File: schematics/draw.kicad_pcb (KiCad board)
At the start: 2 copper layers, 50 x 40 mm, 38 parts, among them P1 I2C Conn, P2 UART Conn, P3 Debug Conn, P4 USB_OTG, P5 Power_IN, P6 Power_OUT, SW1 SW_Push, U1 EFM32HG309, U2 TPD4E002, U3 INA260

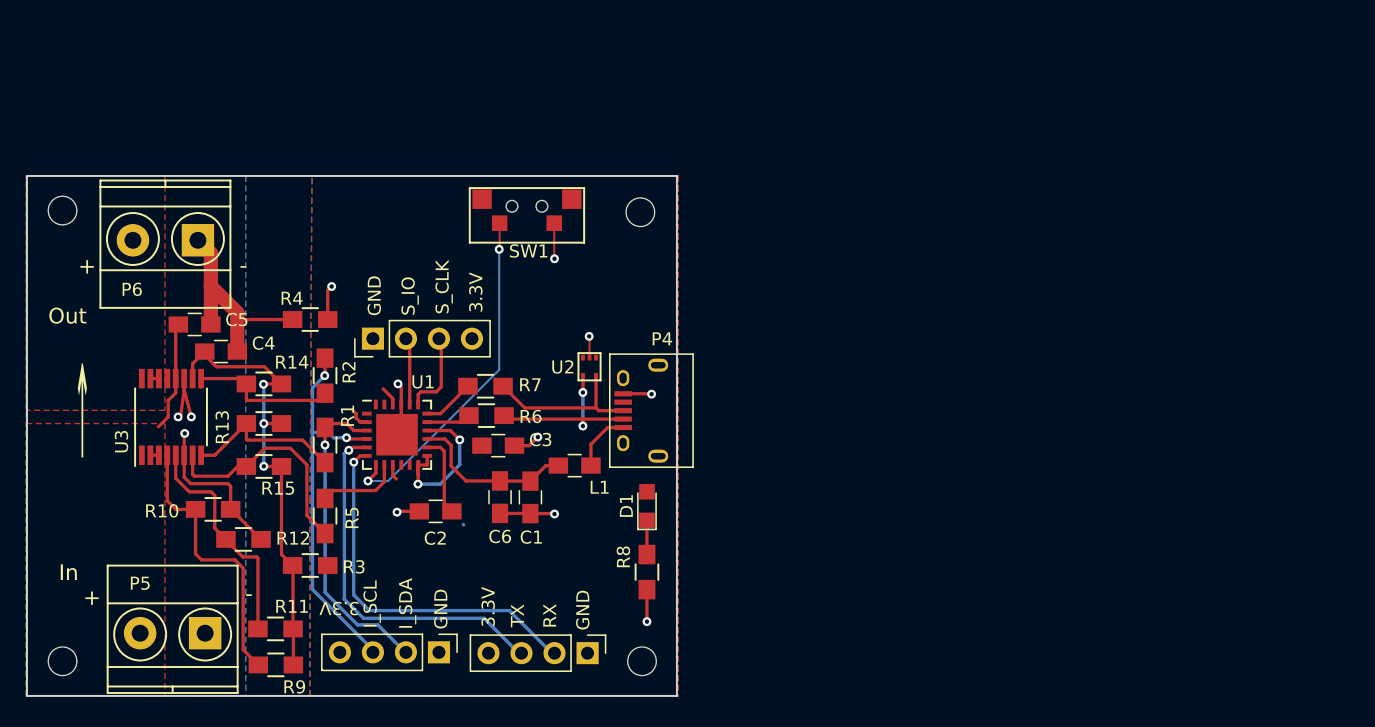
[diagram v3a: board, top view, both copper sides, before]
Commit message: updating footprint assignment
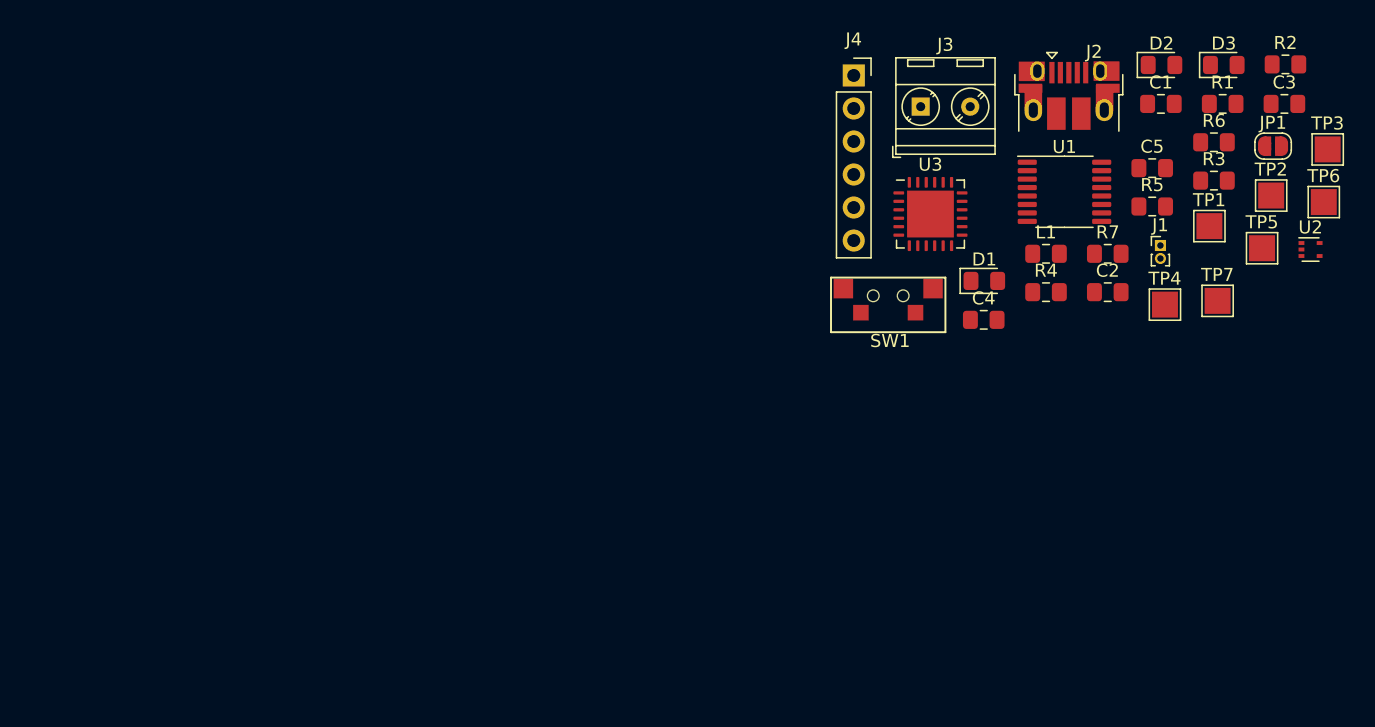
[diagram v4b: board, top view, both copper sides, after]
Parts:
- removed C6: 1nF, Capacitors_SMD:C_0805_HandSoldering
- removed P1: I2C Conn, Pin_Headers:Pin_Header_Straight_1x04_Pitch2.54mm
- removed P2: UART Conn, Pin_Headers:Pin_Header_Straight_1x04_Pitch2.54mm
- removed P3: Debug Conn, Pin_Headers:Pin_Header_Straight_1x04_Pitch2.54mm
- removed P4: USB_OTG, Connect:USB_Micro-B
- removed P5: Power_IN, Terminal_Blocks:TerminalBlock_Pheonix_MKDS1.5-2pol
- removed P6: Power_OUT, Terminal_Blocks:TerminalBlock_Pheonix_MKDS1.5-2pol
- removed R10, R12: 0R, Resistors_SMD:R_0805_HandSoldering
- removed R11, R9: 0R_NP, Resistors_SMD:R_0805_HandSoldering
- removed R13, R14, R15: 1K, Resistors_SMD:R_0805_HandSoldering
- removed R8: 100R, Resistors_SMD:R_0805_HandSoldering
- removed REF** (x4): MountingHole_2.2mm_M2, Mounting_Holes:MountingHole_2.2mm_M2
- removed REF***: OSHW-Logo_5.7x6mm_SilkScreen, Symbols:OSHW-Logo_5.7x6mm_SilkScreen
- added D2: Diode, Diode_SMD:D_0805_2012Metric_Pad1.15x1.40mm_HandSolder, F.Cu at (147.3, 86.5)
- added D3: LED, LED_SMD:LED_0805_2012Metric_Pad1.15x1.40mm_HandSolder, F.Cu at (152.1, 86.5)
- added J1: Conn_01x02_Female, Connector_PinHeader_1.00mm:PinHeader_1x02_P1.00mm_Vertical, F.Cu at (147.2, 100.3)
- added J2: USB_B_Micro, Connector_USB:USB_Micro-B_Amphenol_10103594-0001LF_Horizontal, F.Cu at (140.2, 88.8)
- added J3: Screw_Terminal_01x02, TerminalBlock_MetzConnect:TerminalBlock_MetzConnect_Type086_RT03402HBLC_1x02_P3.81mm_Horizontal, F.Cu at (128.8, 89.7)
- added J4: Debug Header, Connector_PinSocket_2.54mm:PinSocket_1x06_P2.54mm_Vertical, F.Cu at (123.6, 87.3)
- added JP1: Jumper, Jumper:SolderJumper-2_P1.3mm_Open_RoundedPad1.0x1.5mm, F.Cu at (155.9, 92.7)
- added TP1: TestPoint, TestPoint:TestPoint_Pad_2.0x2.0mm, F.Cu at (151.0, 98.9)
- added TP2: TestPoint, TestPoint:TestPoint_Pad_2.0x2.0mm, F.Cu at (155.7, 96.5)
- added TP3: TestPoint, TestPoint:TestPoint_Pad_2.0x2.0mm, F.Cu at (160.1, 93.0)
- added TP4: TestPoint, TestPoint:TestPoint_Pad_2.0x2.0mm, F.Cu at (147.5, 104.9)
- added TP5: TestPoint, TestPoint:TestPoint_Pad_2.0x2.0mm, F.Cu at (155.0, 100.6)
- added TP6: TestPoint, TestPoint:TestPoint_Pad_2.0x2.0mm, F.Cu at (159.8, 97.0)
- added TP7: TestPoint, TestPoint:TestPoint_Pad_2.0x2.0mm, F.Cu at (151.6, 104.6)
- C1: value 4.7uF -> 0.1uF; footprint Capacitors_SMD:C_0805_HandSoldering -> Capacitor_SMD:C_0805_2012Metric_Pad1.15x1.40mm_HandSolder
- C2: value 1uF -> 1nF; footprint Capacitors_SMD:C_0805_HandSoldering -> Capacitor_SMD:C_0805_2012Metric_Pad1.15x1.40mm_HandSolder
- C3: value 1uF -> 4.7uF; footprint Capacitors_SMD:C_0805_HandSoldering -> Capacitor_SMD:C_0805_2012Metric_Pad1.15x1.40mm_HandSolder
- C4: value 0.1uF -> 1uF; footprint Capacitors_SMD:C_0805_HandSoldering -> Capacitor_SMD:C_0805_2012Metric_Pad1.15x1.40mm_HandSolder
- C5: footprint Capacitors_SMD:C_0805_HandSoldering -> Capacitor_SMD:C_0805_2012Metric_Pad1.15x1.40mm_HandSolder
- D1: footprint LEDs:LED_0805 -> LED_SMD:LED_0805_2012Metric_Pad1.15x1.40mm_HandSolder
- L1: footprint Capacitors_SMD:C_0805_HandSoldering -> Inductor_SMD:L_0805_2012Metric_Pad1.15x1.40mm_HandSolder
- R1, R2: value 0R -> 15R; footprint Resistors_SMD:R_0805_HandSoldering -> Resistor_SMD:R_0805_2012Metric_Pad1.15x1.40mm_HandSolder
- R3, R4, R5: value 0R -> 4K7; footprint Resistors_SMD:R_0805_HandSoldering -> Resistor_SMD:R_0805_2012Metric_Pad1.15x1.40mm_HandSolder
- R6, R7: value 15R -> 1K; footprint Resistors_SMD:R_0805_HandSoldering -> Resistor_SMD:R_0805_2012Metric_Pad1.15x1.40mm_HandSolder
- U1: value EFM32HG309 -> INA260; footprint Housings_DFN_QFN:QFN-24-1EP_5x5mm_Pitch0.65mm -> Package_SO:TSSOP-16_4.4x5mm_P0.65mm
- U2: footprint TO_SOT_Packages_SMD:SOT-553 -> Package_TO_SOT_SMD:SOT-553
- U3: value INA260 -> EFM32HG309; footprint Housings_SSOP:TSSOP-16_4.4x5mm_Pitch0.65mm -> Package_DFN_QFN:QFN-24-1EP_5x5mm_P0.65mm_EP3.6x3.6mm
- moved R2 77.7 mm to (156.8, 86.4), turned to 0 degrees
- moved R3 75.6 mm to (151.3, 95.4), turned to 0 degrees
- moved C5 74.6 mm to (146.6, 94.4)
- moved R1 73.9 mm to (152.0, 89.5), turned to 0 degrees
- moved R5 67.9 mm to (146.6, 97.3), turned to 0 degrees
- moved C3 65.9 mm to (156.7, 89.5)
- moved U3 60.4 mm to (129.5, 97.9), turned to 0 degrees
- moved R6 59.8 mm to (151.3, 92.4), turned to 0 degrees
- moved C4 58.7 mm to (133.6, 106.1)
- moved C1 57.2 mm to (147.2, 89.5), turned to 0 degrees
- moved R4 56.6 mm to (138.4, 103.9), turned to 0 degrees
- moved U2 56.2 mm to (158.7, 100.7), turned to 0 degrees
- moved U1 54.6 mm to (139.8, 96.2)
- moved C2 54.4 mm to (143.1, 103.9), turned to 0 degrees
- moved R7 48.9 mm to (143.1, 101.0), turned to 0 degrees
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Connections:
- C1 pad 1: Net-(C1-Pad1) -> +3V3
- C2 pad 1: Net-(C2-Pad1) -> +3V3
- C4 pad 1: +3.3VA -> +3V3
- C4 pad 2: GNDA -> GND
- C5 pad 2: GNDA -> GND
- L1 pad 2: Net-(C1-Pad1) -> USB_5V
- R1 pad 1: /MCU/I2C0-SDA -> Net-(J2-Pad3)
- R1 pad 2: /Current Sense Amplifier/I2C_SDA -> USB_DP
- R2 pad 1: /MCU/I2C0_SCL -> Net-(J2-Pad2)
- R2 pad 2: /Current Sense Amplifier/I2C_SCL -> USB_DM
- R3 pad 1: +3V3 -> Net-(R3-Pad1)
- R3 pad 2: +3.3VA -> I2C_SDA
- R4 pad 1: GND -> Net-(R3-Pad1)
- R4 pad 2: GNDA -> I2C_SCL
- R5 pad 1: /MCU/GPIO_PB11 -> Net-(R3-Pad1)
- R5 pad 2: /Current Sense Amplifier/ALERT -> ALERT
- R6 pad 1: Net-(P4-Pad2) -> Net-(D1-Pad1)
- R6 pad 2: Net-(R6-Pad2) -> GND
- R7 pad 1: Net-(P4-Pad3) -> Net-(D3-Pad2)
- SW1 pad 1: Net-(SW1-Pad1) -> Net-(J4-Pad5)
- U1 pad 1: Net-(U1-Pad1) -> Net-(J3-Pad1)
- U1 pad 10: Net-(U1-Pad10) -> +3V3
- U1 pad 11: Net-(U1-Pad11) -> GND
- U1 pad 12: +3V3 -> Net-(J1-Pad2)
- U1 pad 13: +3V3 -> (no net)
- U1 pad 14: Net-(C2-Pad1) -> Net-(J3-Pad2)
- U1 pad 15: Net-(C1-Pad1) -> Net-(J3-Pad2)
- U1 pad 16: +3V3 -> Net-(J3-Pad2)
- U1 pad 2: +3V3 -> Net-(J3-Pad1)
- U1 pad 3: /MCU/I2C0-SDA -> Net-(J3-Pad1)
- U1 pad 4: /MCU/I2C0_SCL -> GND
- U1 pad 5: /MCU/UART_TX -> GND
- U1 pad 6: Net-(P2-Pad2) -> GND
- U1 pad 7: Net-(SW1-Pad1) -> ALERT
- U1 pad 8: /MCU/GPIO_PB11 -> I2C_SDA
- U1 pad 9: +3V3 -> I2C_SCL
- U2 pad 1: Net-(U2-Pad1) -> Net-(J2-Pad3)
- U2 pad 3: Net-(U2-Pad3) -> Net-(J2-Pad2)
- U2 pad 4: Net-(P4-Pad2) -> (no net)
- U2 pad 5: Net-(P4-Pad3) -> (no net)
- U3 pad 1: Net-(C5-Pad1) -> Net-(R7-Pad2)
- U3 pad 10: +3.3VA -> Net-(TP6-Pad1)
- U3 pad 11: GNDA -> ALERT
- U3 pad 12: Net-(C5-Pad1) -> +3V3
- U3 pad 13: Net-(U3-Pad13) -> +3V3
- U3 pad 14: Net-(P6-Pad2) -> Net-(C5-Pad1)
- U3 pad 15: Net-(P6-Pad2) -> USB_5V
- U3 pad 16: Net-(P6-Pad2) -> Net-(D2-Pad2)
- U3 pad 2: Net-(C5-Pad1) -> +3V3
- U3 pad 3: Net-(C5-Pad1) -> I2C_SDA
- U3 pad 4: Net-(R10-Pad1) -> I2C_SCL
- U3 pad 6: GNDA -> Net-(TP3-Pad1)
- U3 pad 7: /Current Sense Amplifier/ALERT -> Net-(J4-Pad5)
- U3 pad 8: /Current Sense Amplifier/I2C_SDA -> Net-(TP4-Pad1)
- U3 pad 9: /Current Sense Amplifier/I2C_SCL -> +3V3
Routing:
- net +3.3VA: track 36.5 -> 0.00 mm, vias 3 -> 0
- net GNDA: track 34.7 -> 0.00 mm, vias 3 -> 0
- net /MCU/I2C0_SCL: track 29.3 -> 0.00 mm, vias 2 -> 0
- net Net-(P2-Pad2): track 28.5 -> 0.00 mm, vias 1 -> 0
- net /MCU/UART_TX: track 28.3 -> 0.00 mm, vias 1 -> 0
- net GND: track 28.1 -> 0.00 mm, vias 9 -> 0
- net Net-(SW1-Pad1): track 26.5 -> 0.00 mm, vias 2 -> 0
- net /MCU/I2C0-SDA: track 24.3 -> 0.00 mm, vias 1 -> 0
- net Net-(R10-Pad1): track 21.4 -> 0.00 mm
- net /Current Sense Amplifier/ALERT: track 17.6 -> 0.00 mm
- net Net-(TP2-Pad1): track 17.6 -> 0.00 mm
- net +3V3: track 17.2 -> 0.00 mm, vias 2 -> 0
- net Net-(P4-Pad2): track 13.7 -> 0.00 mm, vias 2 -> 0
- net Net-(C1-Pad1): track 12.9 -> 0.00 mm
- net /Current Sense Amplifier/I2C_SDA: track 12.5 -> 0.00 mm
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- removed copper zone on F.Cu, net +3V3
- removed copper zone on B.Cu, net GND
- removed copper zone on B.Cu, net GNDA
- removed copper zone on F.Cu, net Net-(C5-Pad1)
- removed copper zone on F.Cu, net Net-(P6-Pad2)
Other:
- board outline removed
- board text removed: "+"
- board text removed: "-"
- board text removed: "3.3V"
- board text removed: "GND"
- board text removed: "I_SCL"
- board text removed: "I_SDA"
- board text removed: "In"
- board text removed: "Out"
- board text removed: "RX"
- board text removed: "S_CLK"
- board text removed: "S_IO"
- board text removed: "TX"
- board text removed: "chinmay.audio/draw"
- board text removed: "draw v1.1 14/3/2017"
- board text removed: "↑"
